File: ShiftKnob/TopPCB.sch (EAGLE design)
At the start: 6 parts

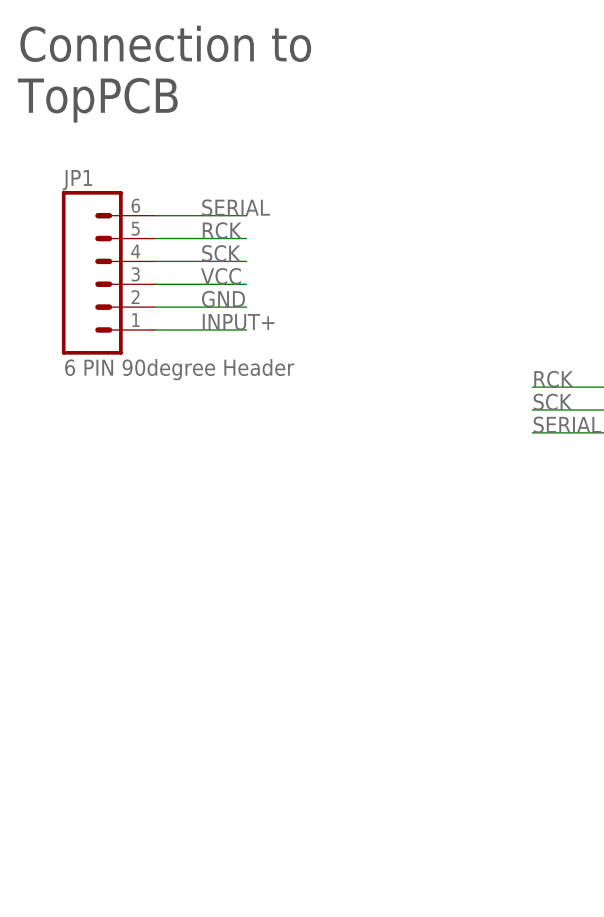
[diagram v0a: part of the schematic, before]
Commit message: use (2) 4 pin connectors rather than a 6 pin connector. Board layout and schematic preliminarily complete.
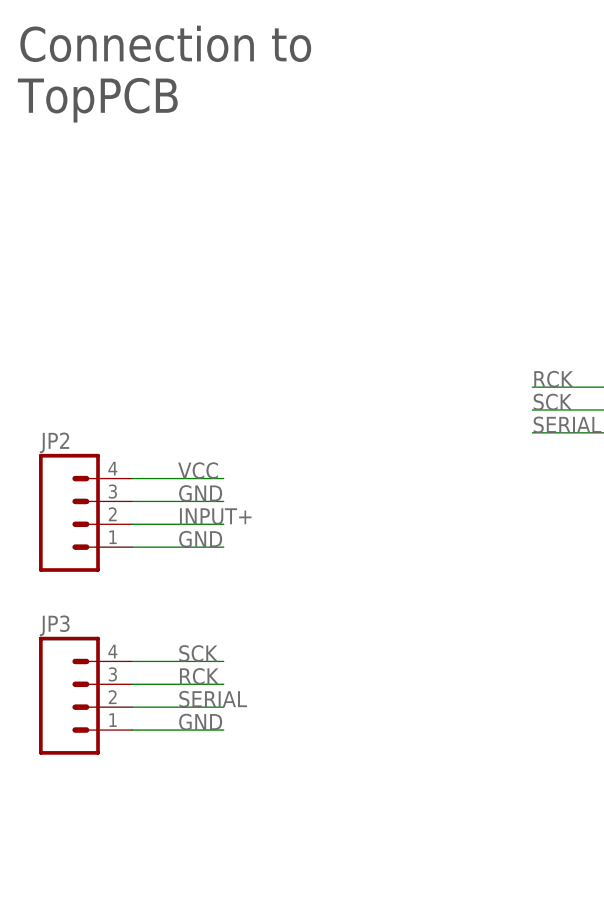
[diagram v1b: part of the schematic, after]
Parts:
- removed JP1: 6 PIN 90degree Header, SparkFun-Connectors:M06SIP
- added JP2, JP3: (no value), SparkFun-Connectors:M04PTH
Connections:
- net GND: now also JP2.1, JP2.3, JP3.1; no longer JP1.2
- net INPUT+: now also JP2.2; no longer JP1.1
- net RCK: now also JP3.3; no longer JP1.5
- net SCK: now also JP3.4; no longer JP1.4
- net SERIAL: now also JP3.2; no longer JP1.6
- net VCC: now also JP2.4; no longer JP1.3
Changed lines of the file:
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@@
 <layers>
 <layer number="1" name="Top" color="4" fill="1" visible="no" active="no"/>
+<layer number="2" name="Route2" color="1" fill="3" visible="no" active="no"/>
+<layer number="3" name="Route3" color="4" fill="3" visible="no" active="no"/>
+<layer number="14" name="Route14" color="1" fill="6" visible="no" active="no"/>
+<layer number="15" name="Route15" color="4" fill="6" visible="no" active="no"/>
 <layer number="16" name="Bottom" color="1" fill="1" visible="no" active="no"/>
 <layer number="17" name="Pads" color="2" fill="1" visible="no" active="no"/>
@@
 <part name="FRAME1" library="FORD_frames" deviceset="FRAME_A_L" device=""/>
 <part name="GND3" library="SparkFun-Aesthetics" deviceset="GND" device=""/>
-<part name="JP1" library="SparkFun-Connectors" deviceset="M06" device="SIP" value="6 PIN 90degree Header"/>
 <part name="C1" library="SparkFun-Capacitors" deviceset="CAP" device="0402-CAP" value="0.1uF"/>
 <part name="GND4" library="SparkFun-Aesthetics" deviceset="GND" device=""/>
 <part name="ARRAY1" library="resistor-array" deviceset="744-8" device="" value="220"/>
 <part name="ARRAY2" library="resistor-array" deviceset="744-8" device="" value="220"/>
+<part name="JP2" library="SparkFun-Connectors" deviceset="M04" device="PTH"/>
+<part name="JP3" library="SparkFun-Connectors" deviceset="M04" device="PTH"/>
 </parts>
 <sheets>
@@
 <instance part="FRAME1" gate="G$2" x="172.72" y="0"/>
 <instance part="GND3" gate="1" x="116.84" y="111.76"/>
-<instance part="JP1" gate="G$1" x="38.1" y="97.79"/>
 <instance part="C1" gate="G$1" x="105.41" y="99.06"/>
 <instance part="GND4" gate="1" x="105.41" y="93.98"/>
 <instance part="ARRAY1" gate="G$1" x="186.69" y="116.84"/>
 <instance part="ARRAY2" gate="G$1" x="186.69" y="96.52"/>
+<instance part="JP2" gate="G$1" x="35.56" y="71.12"/>
+<instance part="JP3" gate="G$1" x="35.56" y="50.8"/>
 </instances>
 <busses>
@@
 </segment>
 <segment>
-<pinref part="JP1" gate="G$1" pin="1"/>
-<wire x1="43.18" y1="92.71" x2="53.34" y2="92.71" width="0.1524" layer="91"/>
-<label x="48.26" y="92.71" size="1.778" layer="95"/>
+<pinref part="JP2" gate="G$1" pin="2"/>
+<wire x1="40.64" y1="71.12" x2="50.8" y2="71.12" width="0.1524" layer="91"/>
+<label x="45.72" y="71.12" size="1.778" layer="95"/>
 </segment>
 </net>
@@
 </segment>
 <segment>
-<pinref part="JP1" gate="G$1" pin="2"/>
-<wire x1="43.18" y1="95.25" x2="53.34" y2="95.25" width="0.1524" layer="91"/>
-<label x="48.26" y="95.25" size="1.778" layer="95"/>
+<pinref part="JP2" gate="G$1" pin="3"/>
+<wire x1="40.64" y1="73.66" x2="50.8" y2="73.66" width="0.1524" layer="91"/>
+<label x="45.72" y="73.66" size="1.778" layer="95"/>
+</segment>
+<segment>
+<pinref part="JP2" gate="G$1" pin="1"/>
+<wire x1="40.64" y1="68.58" x2="50.8" y2="68.58" width="0.1524" layer="91"/>
+<label x="45.72" y="68.58" size="1.778" layer="95"/>
+</segment>
+<segment>
+<pinref part="JP3" gate="G$1" pin="1"/>
+<wire x1="40.64" y1="48.26" x2="50.8" y2="48.26" width="0.1524" layer="91"/>
+<label x="45.72" y="48.26" size="1.778" layer="95"/>
 </segment>
 </net>
@@
 </segment>
 <segment>
-<pinref part="JP1" gate="G$1" pin="5"/>
-<wire x1="43.18" y1="102.87" x2="53.34" y2="102.87" width="0.1524" layer="91"/>
-<label x="48.26" y="102.87" size="1.778" layer="95"/>
+<pinref part="JP3" gate="G$1" pin="3"/>
+<wire x1="40.64" y1="53.34" x2="50.8" y2="53.34" width="0.1524" layer="91"/>
+<label x="45.72" y="53.34" size="1.778" layer="95"/>
 </segment>
 </net>
@@
 </segment>
 <segment>
-<pinref part="JP1" gate="G$1" pin="4"/>
-<wire x1="43.18" y1="100.33" x2="53.34" y2="100.33" width="0.1524" layer="91"/>
-<label x="48.26" y="100.33" size="1.778" layer="95"/>
+<pinref part="JP3" gate="G$1" pin="4"/>
+<wire x1="40.64" y1="55.88" x2="50.8" y2="55.88" width="0.1524" layer="91"/>
+<label x="45.72" y="55.88" size="1.778" layer="95"/>
 </segment>
 </net>
@@
 </segment>
 <segment>
-<pinref part="JP1" gate="G$1" pin="6"/>
-<wire x1="43.18" y1="105.41" x2="53.34" y2="105.41" width="0.1524" layer="91"/>
-<label x="48.26" y="105.41" size="1.778" layer="95"/>
+<pinref part="JP3" gate="G$1" pin="2"/>
+<wire x1="40.64" y1="50.8" x2="50.8" y2="50.8" width="0.1524" layer="91"/>
+<label x="45.72" y="50.8" size="1.778" layer="95"/>
 </segment>
 </net>
@@
 </segment>
 <segment>
-<pinref part="JP1" gate="G$1" pin="3"/>
-<wire x1="43.18" y1="97.79" x2="53.34" y2="97.79" width="0.1524" layer="91"/>
-<label x="48.26" y="97.79" size="1.778" layer="95"/>
-</segment>
-</net>
+<pinref part="JP2" gate="G$1" pin="4"/>
+<wire x1="40.64" y1="76.2" x2="50.8" y2="76.2" width="0.1524" layer="91"/>
+<label x="45.72" y="76.2" size="1.778" layer="95"/>
+</segment>
+</net>

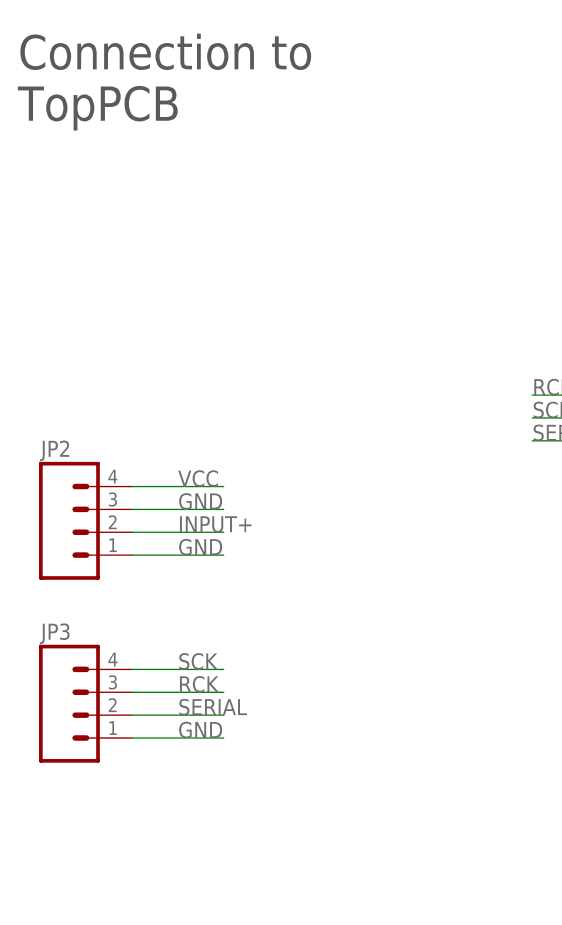
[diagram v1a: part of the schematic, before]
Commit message: redo silk screen pin labels. DRC checks out OK.
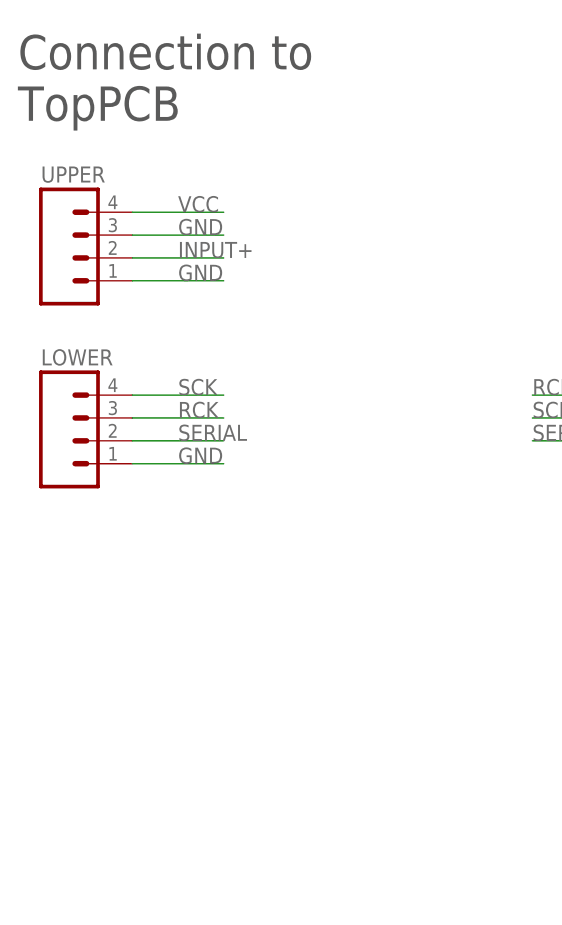
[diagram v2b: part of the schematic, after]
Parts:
- removed JP2, JP3: (no value), SparkFun-Connectors:M04PTH
- added LOWER, UPPER: (no value), SparkFun-Connectors:M04PTH
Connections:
- net GND: now also LOWER.1, UPPER.1, UPPER.3; no longer JP2.1, JP2.3, JP3.1
- net INPUT+: now also UPPER.2; no longer JP2.2
- net RCK: now also LOWER.3; no longer JP3.3
- net SCK: now also LOWER.4; no longer JP3.4
- net SERIAL: now also LOWER.2; no longer JP3.2
- net VCC: now also UPPER.4; no longer JP2.4
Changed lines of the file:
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@@
 <part name="ARRAY1" library="resistor-array" deviceset="744-8" device="" value="220"/>
 <part name="ARRAY2" library="resistor-array" deviceset="744-8" device="" value="220"/>
-<part name="JP2" library="SparkFun-Connectors" deviceset="M04" device="PTH"/>
-<part name="JP3" library="SparkFun-Connectors" deviceset="M04" device="PTH"/>
+<part name="UPPER" library="SparkFun-Connectors" deviceset="M04" device="PTH"/>
+<part name="LOWER" library="SparkFun-Connectors" deviceset="M04" device="PTH"/>
 </parts>
 <sheets>
@@
 <instance part="ARRAY1" gate="G$1" x="186.69" y="116.84"/>
 <instance part="ARRAY2" gate="G$1" x="186.69" y="96.52"/>
-<instance part="JP2" gate="G$1" x="35.56" y="71.12"/>
-<instance part="JP3" gate="G$1" x="35.56" y="50.8"/>
+<instance part="UPPER" gate="G$1" x="35.56" y="101.6"/>
+<instance part="LOWER" gate="G$1" x="35.56" y="81.28"/>
 </instances>
 <busses>
@@
 </segment>
 <segment>
-<pinref part="JP2" gate="G$1" pin="2"/>
-<wire x1="40.64" y1="71.12" x2="50.8" y2="71.12" width="0.1524" layer="91"/>
-<label x="45.72" y="71.12" size="1.778" layer="95"/>
+<pinref part="UPPER" gate="G$1" pin="2"/>
+<wire x1="40.64" y1="101.6" x2="50.8" y2="101.6" width="0.1524" layer="91"/>
+<label x="45.72" y="101.6" size="1.778" layer="95"/>
 </segment>
 </net>
@@
 </segment>
 <segment>
-<pinref part="JP2" gate="G$1" pin="3"/>
-<wire x1="40.64" y1="73.66" x2="50.8" y2="73.66" width="0.1524" layer="91"/>
-<label x="45.72" y="73.66" size="1.778" layer="95"/>
-</segment>
-<segment>
-<pinref part="JP2" gate="G$1" pin="1"/>
-<wire x1="40.64" y1="68.58" x2="50.8" y2="68.58" width="0.1524" layer="91"/>
-<label x="45.72" y="68.58" size="1.778" layer="95"/>
-</segment>
-<segment>
-<pinref part="JP3" gate="G$1" pin="1"/>
-<wire x1="40.64" y1="48.26" x2="50.8" y2="48.26" width="0.1524" layer="91"/>
-<label x="45.72" y="48.26" size="1.778" layer="95"/>
+<pinref part="UPPER" gate="G$1" pin="3"/>
+<wire x1="40.64" y1="104.14" x2="50.8" y2="104.14" width="0.1524" layer="91"/>
+<label x="45.72" y="104.14" size="1.778" layer="95"/>
+</segment>
+<segment>
+<pinref part="UPPER" gate="G$1" pin="1"/>
+<wire x1="40.64" y1="99.06" x2="50.8" y2="99.06" width="0.1524" layer="91"/>
+<label x="45.72" y="99.06" size="1.778" layer="95"/>
+</segment>
+<segment>
+<pinref part="LOWER" gate="G$1" pin="1"/>
+<wire x1="40.64" y1="78.74" x2="50.8" y2="78.74" width="0.1524" layer="91"/>
+<label x="45.72" y="78.74" size="1.778" layer="95"/>
 </segment>
 </net>
@@
 </segment>
 <segment>
-<pinref part="JP3" gate="G$1" pin="3"/>
-<wire x1="40.64" y1="53.34" x2="50.8" y2="53.34" width="0.1524" layer="91"/>
-<label x="45.72" y="53.34" size="1.778" layer="95"/>
+<pinref part="LOWER" gate="G$1" pin="3"/>
+<wire x1="40.64" y1="83.82" x2="50.8" y2="83.82" width="0.1524" layer="91"/>
+<label x="45.72" y="83.82" size="1.778" layer="95"/>
 </segment>
 </net>
@@
 </segment>
 <segment>
-<pinref part="JP3" gate="G$1" pin="4"/>
-<wire x1="40.64" y1="55.88" x2="50.8" y2="55.88" width="0.1524" layer="91"/>
-<label x="45.72" y="55.88" size="1.778" layer="95"/>
+<pinref part="LOWER" gate="G$1" pin="4"/>
+<wire x1="40.64" y1="86.36" x2="50.8" y2="86.36" width="0.1524" layer="91"/>
+<label x="45.72" y="86.36" size="1.778" layer="95"/>
 </segment>
 </net>
@@
 </segment>
 <segment>
-<pinref part="JP3" gate="G$1" pin="2"/>
-<wire x1="40.64" y1="50.8" x2="50.8" y2="50.8" width="0.1524" layer="91"/>
-<label x="45.72" y="50.8" size="1.778" layer="95"/>
+<pinref part="LOWER" gate="G$1" pin="2"/>
+<wire x1="40.64" y1="81.28" x2="50.8" y2="81.28" width="0.1524" layer="91"/>
+<label x="45.72" y="81.28" size="1.778" layer="95"/>
 </segment>
 </net>
@@
 </segment>
 <segment>
-<pinref part="JP2" gate="G$1" pin="4"/>
-<wire x1="40.64" y1="76.2" x2="50.8" y2="76.2" width="0.1524" layer="91"/>
-<label x="45.72" y="76.2" size="1.778" layer="95"/>
+<pinref part="UPPER" gate="G$1" pin="4"/>
+<wire x1="40.64" y1="106.68" x2="50.8" y2="106.68" width="0.1524" layer="91"/>
+<label x="45.72" y="106.68" size="1.778" layer="95"/>
 </segment>
 </net>
@@
 </sheet>
 </sheets>
+<errors>
+</errors>
 </schematic>
 </drawing>

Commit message: add v02 and v01 docs.
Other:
- note added: "02"
- note removed: "01"
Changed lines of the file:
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@@
 <sheet>
 <plain>
-<text x="266.7" y="8.89" size="3.81" layer="94">01</text>
+<text x="266.7" y="8.89" size="3.81" layer="94">02</text>
 <text x="190.5" y="7.62" size="3.81" layer="94">Zachary Nelson
 znelson1@ford.com</text>
